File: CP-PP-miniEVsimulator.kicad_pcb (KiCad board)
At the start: 2 copper layers, 69.8 x 34 mm, 103 parts, among them J1 Conn_01x01_Female, J2 Conn_01x01_Female, J3 Conn_01x01_Female

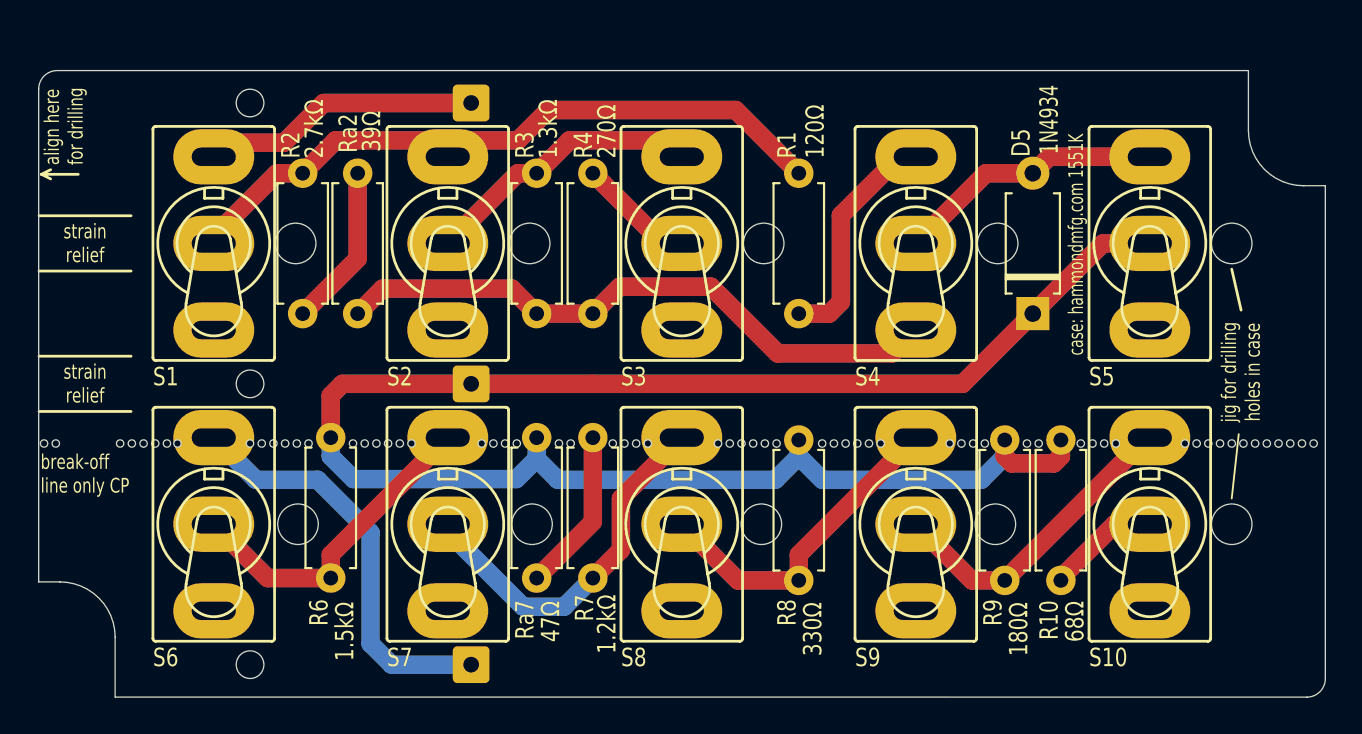
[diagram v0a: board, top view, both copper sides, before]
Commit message: cutouts mirrored
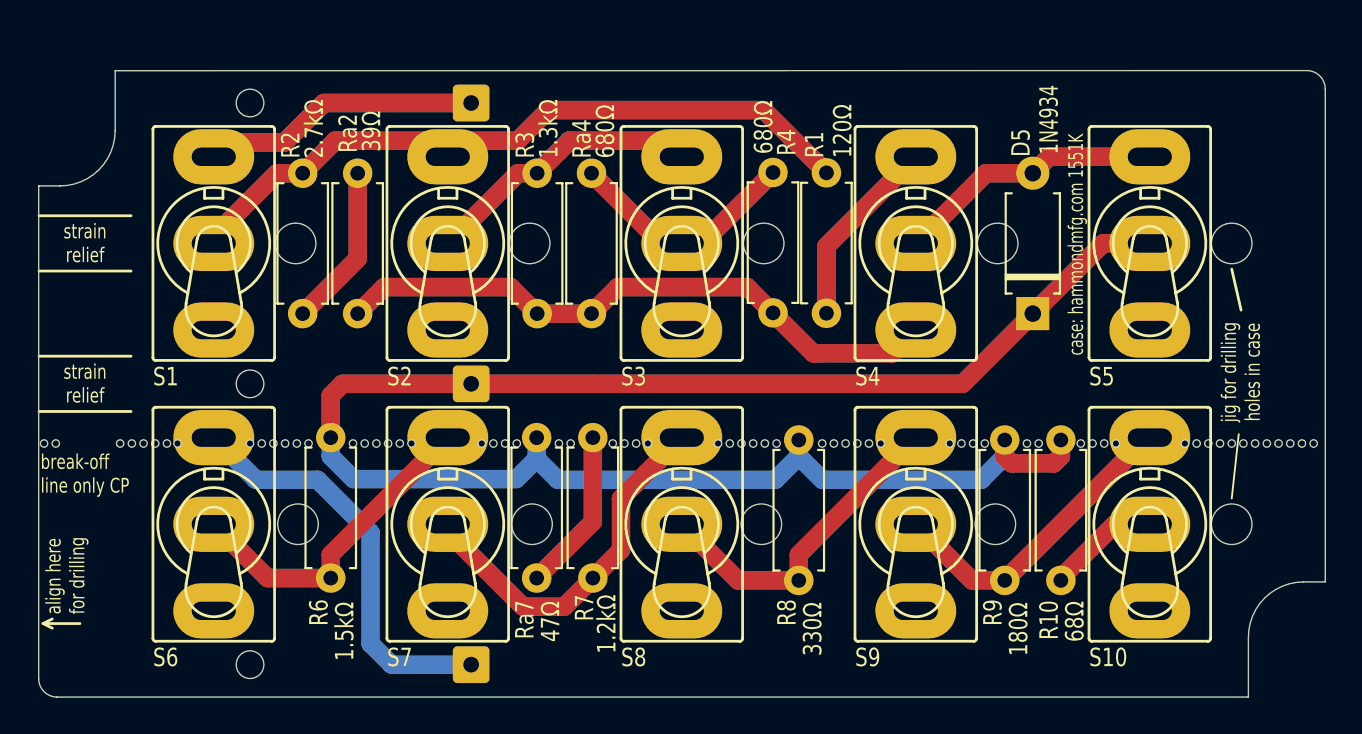
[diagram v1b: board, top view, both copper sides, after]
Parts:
- added R4: 680Ω, Resistor_THT:R_Axial_DIN0207_L6.3mm_D2.5mm_P7.62mm_Horizontal, F.Cu at (131.9, 135.8)
- Ra4: renamed from R4; value 270Ω -> 680Ω
- moved R1 1.50 mm to (134.8, 135.9)
- moved Ra4 0.07 mm to (122.1, 135.9)
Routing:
- net Net-(R4-Pad2): track 12.8 -> 26.0 mm
- net Net-(R7-Pad2): track 20.2 -> 30.8 mm
- net Net-(R1-Pad1): track 25.3 -> 21.0 mm
- net Net-(R1-Pad2): track 74.3 -> 77.7 mm
- net Net-(R3-Pad2): track 30.8 -> 32.0 mm
- net /CP: track 30.5 -> 31.6 mm
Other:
- outline, holes or cut-outs redrawn
